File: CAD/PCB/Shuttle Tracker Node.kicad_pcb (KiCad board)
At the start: 2 copper layers, 90.8 x 45.7 mm, 23 parts, among them J1 Conn_01x01, J2 Conn_01x01, J3 Conn_01x01, J4 Conn_01x01, J5 Conn_01x01, J6 Conn_01x01, J7 Conn_01x01, SW1 SW_Push, SW10 SW_Push, SW11 SW_Push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

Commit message: Added Mounting Holes
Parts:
- added REF**: MountingHole_3.2mm_M3, MountingHole:MountingHole_3.2mm_M3, F.Cu at (128.5, 79.8)
- added REF**: MountingHole_3.2mm_M3, MountingHole:MountingHole_3.2mm_M3, F.Cu at (128.5, 118.4)
- added REF**: MountingHole_3.2mm_M3, MountingHole:MountingHole_3.2mm_M3, F.Cu at (226.6, 79.8)
- added REF**: MountingHole_3.2mm_M3, MountingHole:MountingHole_3.2mm_M3, F.Cu at (226.6, 118.4)
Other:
- board size 90.8 x 45.7 mm -> 105.2 x 45.7 mm
- board text added: "1.0.2"
- board text removed: "1.0.1"
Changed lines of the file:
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@@
     )
+  )
+  (footprint "MountingHole:MountingHole_3.2mm_M3" (layer "F.Cu")
+    (at 128.524 79.756)
+    (descr "Mounting Hole 3.2mm, no annular, M3")
+    (tags "mounting hole 3.2mm no annular m3")
+    (attr exclude_from_pos_files exclude_from_bom)
+    (fp_text reference "REF**" (at 0 -4.2) (layer "F.SilkS") hide
+      (effects (font (size 1 1) (thickness 0.15)))
+    )
+    (fp_text value "MountingHole_3.2mm_M3" (at 0 4.2) (layer "F.Fab")
+      (effects (font (size 1 1) (thickness 0.15)))
+    )
+    (fp_text user "${REFERENCE}" (at 0 0) (layer "F.Fab")
+      (effects (font (size 1 1) (thickness 0.15)))
+    )
+    (fp_circle (center 0 0) (end 3.2 0) (layer "Cmts.User") (width 0.15) (fill none))
+    (fp_circle (center 0 0) (end 3.45 0) (layer "F.CrtYd") (width 0.05) (fill none))
+    (pad "" np_thru_hole circle (at 0 0) (size 3.2 3.2) (drill 3.2) (layers F&B.Cu *.Mask))
+  )
+  (footprint "MountingHole:MountingHole_3.2mm_M3" (layer "F.Cu")
+    (at 128.524 118.364)
+    (descr "Mounting Hole 3.2mm, no annular, M3")
+    (tags "mounting hole 3.2mm no annular m3")
+    (attr exclude_from_pos_files exclude_from_bom)
+    (fp_text reference "REF**" (at 0 -4.2) (layer "F.SilkS") hide
+      (effects (font (size 1 1) (thickness 0.15)))
+    )
+    (fp_text value "MountingHole_3.2mm_M3" (at 0 4.2) (layer "F.Fab")
+      (effects (font (size 1 1) (thickness 0.15)))
+    )
+    (fp_text user "${REFERENCE}" (at 0 0) (layer "F.Fab")
+      (effects (font (size 1 1) (thickness 0.15)))
+    )
+    (fp_circle (center 0 0) (end 3.2 0) (layer "Cmts.User") (width 0.15) (fill none))
+    (fp_circle (center 0 0) (end 3.45 0) (layer "F.CrtYd") (width 0.05) (fill none))
+    (pad "" np_thru_hole circle (at 0 0) (size 3.2 3.2) (drill 3.2) (layers F&B.Cu *.Mask))
   )
   (footprint "B3F-1056:B3F-1056" (layer "F.Cu")
@@
     )
   )
+  (footprint "MountingHole:MountingHole_3.2mm_M3" (layer "F.Cu")
+    (at 226.568 79.756)
+    (descr "Mounting Hole 3.2mm, no annular, M3")
+    (tags "mounting hole 3.2mm no annular m3")
+    (attr exclude_from_pos_files exclude_from_bom)
+    (fp_text reference "REF**" (at 0 -4.2) (layer "F.SilkS") hide
+      (effects (font (size 1 1) (thickness 0.15)))
+    )
+    (fp_text value "MountingHole_3.2mm_M3" (at 0 4.2) (layer "F.Fab")
+      (effects (font (size 1 1) (thickness 0.15)))
+    )
+    (fp_text user "${REFERENCE}" (at 0 0) (layer "F.Fab")
+      (effects (font (size 1 1) (thickness 0.15)))
+    )
+    (fp_circle (center 0 0) (end 3.2 0) (layer "Cmts.User") (width 0.15) (fill none))
+    (fp_circle (center 0 0) (end 3.45 0) (layer "F.CrtYd") (width 0.05) (fill none))
+    (pad "" np_thru_hole circle (at 0 0) (size 3.2 3.2) (drill 3.2) (layers *.Cu *.Mask))
+  )
   (footprint "B3F-1056:B3F-1056" (layer "F.Cu")
     (at 171.45 96.8375)
@@
       (rotate (xyz 0 0 0))
     )
+  )
+  (footprint "MountingHole:MountingHole_3.2mm_M3" (layer "F.Cu")
+    (at 226.568 118.364)
+    (descr "Mounting Hole 3.2mm, no annular, M3")
+    (tags "mounting hole 3.2mm no annular m3")
+    (attr exclude_from_pos_files exclude_from_bom)
+    (fp_text reference "REF**" (at 0 -4.2) (layer "F.SilkS") hide
+      (effects (font (size 1 1) (thickness 0.15)))
+    )
+    (fp_text value "MountingHole_3.2mm_M3" (at 0 4.2) (layer "F.Fab")
+      (effects (font (size 1 1) (thickness 0.15)))
+    )
+    (fp_text user "${REFERENCE}" (at 0 0) (layer "F.Fab")
+      (effects (font (size 1 1) (thickness 0.15)))
+    )
+    (fp_circle (center 0 0) (end 3.2 0) (layer "Cmts.User") (width 0.15) (fill none))
+    (fp_circle (center 0 0) (end 3.45 0) (layer "F.CrtYd") (width 0.05) (fill none))
+    (pad "" np_thru_hole circle (at 0 0) (size 3.2 3.2) (drill 3.2) (layers F&B.Cu *.Mask))
   )
   (footprint "Resistor_THT:R_Axial_DIN0204_L3.6mm_D1.6mm_P5.08mm_Horizontal" (layer "B.Cu")
@@
       (xy 215.927615 106.759896)
     ) (layer "F.SilkS") (width 0) (fill solid))
-  (gr_line (start 222.885 119.38) (end 222.885 78.74) (layer "Edge.Cuts") (width 0.1))
-  (gr_arc (start 134.62 121.92) (mid 132.823949 121.176051) (end 132.08 119.38) (layer "Edge.Cuts") (width 0.1))
-  (gr_arc (start 220.345 76.2) (mid 222.141051 76.943949) (end 222.885 78.74) (layer "Edge.Cuts") (width 0.1))
-  (gr_arc (start 132.08 78.74) (mid 132.823949 76.943949) (end 134.62 76.2) (layer "Edge.Cuts") (width 0.1))
-  (gr_line (start 132.08 78.74) (end 132.08 119.38) (layer "Edge.Cuts") (width 0.1))
-  (gr_arc (start 222.885 119.38) (mid 222.141051 121.176051) (end 220.345 121.92) (layer "Edge.Cuts") (width 0.1))
-  (gr_line (start 220.345 76.2) (end 134.62 76.2) (layer "Edge.Cuts") (width 0.1))
-  (gr_line (start 134.62 121.92) (end 220.345 121.92) (layer "Edge.Cuts") (width 0.1))
-  (gr_text "1.0.1" (at 208.28 118.11) (layer "F.SilkS")
+  (gr_arc (start 226.568 114.808) (mid 230.124 118.364) (end 226.568 121.92) (layer "Edge.Cuts") (width 0.1))
+  (gr_arc (start 226.568 76.2) (mid 230.124 79.756) (end 226.568 83.312) (layer "Edge.Cuts") (width 0.1))
+  (gr_arc (start 128.524 83.312) (mid 124.968 79.756) (end 128.524 76.2) (layer "Edge.Cuts") (width 0.1))
+  (gr_line (start 226.568 114.808) (end 226.568 83.312) (layer "Edge.Cuts") (width 0.1))
+  (gr_line (start 128.524 83.312) (end 128.524 114.808) (layer "Edge.Cuts") (width 0.1))
+  (gr_arc (start 128.524 121.92) (mid 124.968 118.364) (end 128.524 114.808) (layer "Edge.Cuts") (width 0.1))
+  (gr_line (start 226.568 76.2) (end 128.524 76.2) (layer "Edge.Cuts") (width 0.1))
+  (gr_line (start 128.524 121.92) (end 226.568 121.92) (layer "Edge.Cuts") (width 0.1))
+  (gr_text "1.0.2" (at 208.28 118.11) (layer "F.SilkS")
     (effects (font (size 1 1) (thickness 0.15)))
   )

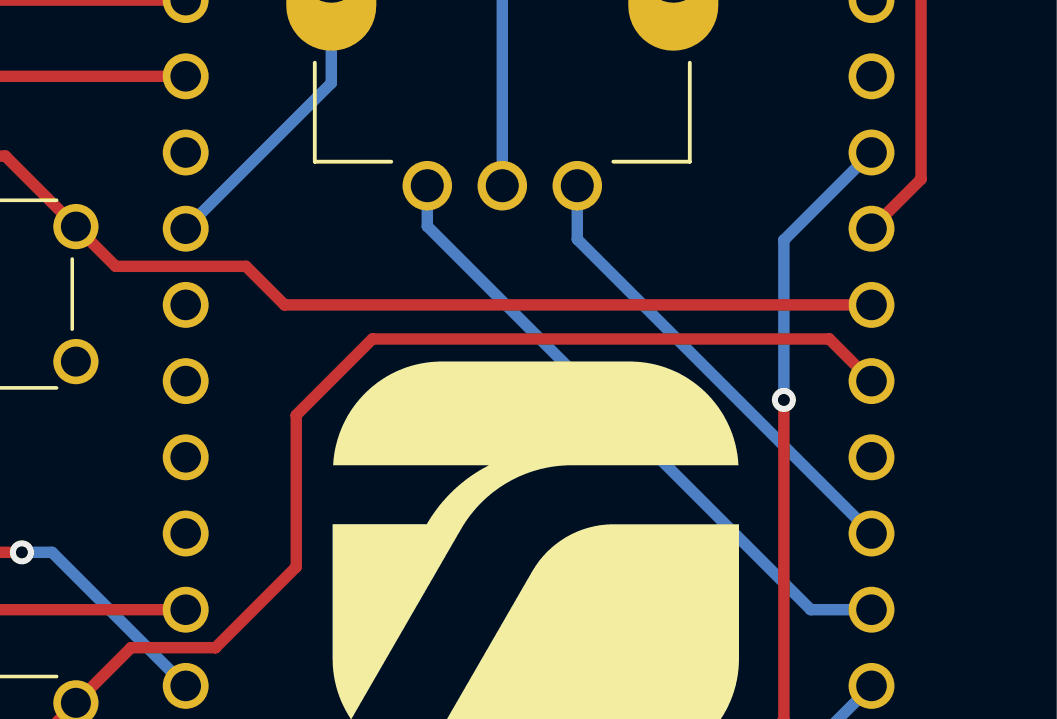
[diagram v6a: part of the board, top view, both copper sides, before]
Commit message: Changed IO Configuration
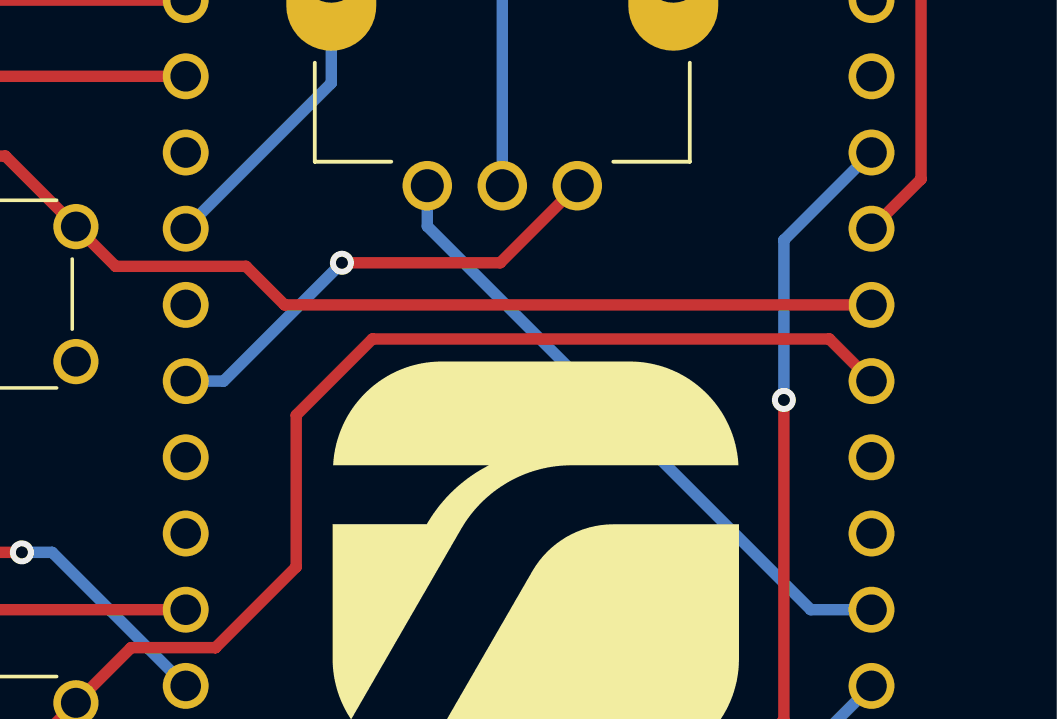
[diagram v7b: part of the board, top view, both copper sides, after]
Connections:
- U1 pad 11: ENC_B -> unconnected-(U1-Pad11)
- U1 pad 22: unconnected-(U1-Pad22) -> ENC_B
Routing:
- net ENC_B: track 15.7 -> 15.8 mm, vias 0 -> 1
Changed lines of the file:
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@@
   (net 24 "unconnected-(U1-Pad20)")
   (net 25 "unconnected-(U1-Pad21)")
-  (net 26 "unconnected-(U1-Pad22)")
-  (net 27 "unconnected-(U1-Pad23)")
-  (net 28 "unconnected-(U1-Pad25)")
-  (net 29 "ENC_GND_A")
-  (net 30 "BAT_5V")
-  (net 31 "BAT_GND")
+  (net 26 "unconnected-(U1-Pad23)")
+  (net 27 "unconnected-(U1-Pad25)")
+  (net 28 "ENC_GND_A")
+  (net 29 "BAT_5V")
+  (net 30 "BAT_GND")
+  (net 31 "unconnected-(U1-Pad11)")
   (footprint "Connector_Pin:Pin_D1.0mm_L10.0mm" (layer "F.Cu")
     (at 135.89 93.95 -90)
@@
     (fp_circle (center 0 0) (end 1 0) (layer "F.Fab") (width 0.12) (fill none))
     (pad "1" thru_hole circle (at 0 0 270) (size 2 2) (drill 1) (layers *.Cu *.Mask)
-      (net 30 "BAT_5V") (pinfunction "Pin_1") (pintype "passive"))
+      (net 29 "BAT_5V") (pinfunction "Pin_1") (pintype "passive"))
     (model "${KICAD6_3DMODEL_DIR}/Connector_Pin.3dshapes/Pin_D1.0mm_L10.0mm.wrl"
       (offset (xyz 0 0 0))
@@
     (fp_circle (center 0 0) (end 0.5 0) (layer "F.Fab") (width 0.12) (fill none))
     (pad "1" thru_hole circle (at 0 0 270) (size 2 2) (drill 1) (layers *.Cu *.Mask)
-      (net 31 "BAT_GND") (pinfunction "Pin_1") (pintype "passive"))
+      (net 30 "BAT_GND") (pinfunction "Pin_1") (pintype "passive"))
     (model "${KICAD6_3DMODEL_DIR}/Connector_Pin.3dshapes/Pin_D1.0mm_L10.0mm.wrl"
       (offset (xyz 0 0 0))
@@
       (net 13 "ENC_B") (pinfunction "B") (pintype "passive"))
     (pad "C" thru_hole circle (at 0 7.5) (size 1.65 1.65) (drill 1.1) (layers *.Cu *.Mask)
-      (net 29 "ENC_GND_A") (pinfunction "C") (pintype "passive"))
+      (net 28 "ENC_GND_A") (pinfunction "C") (pintype "passive"))
     (pad "S1" thru_hole oval (at -5.7 0) (size 3 6) (drill oval 2 2.8) (layers *.Cu *.Mask)
       (net 14 "ENC_SW_IN") (pinfunction "S1") (pintype "passive"))
@@
       (net 20 "unconnected-(U1-Pad10)") (pinfunction "GND") (pintype "power_in"))
     (pad "11" thru_hole circle (at -11.43 -8.0078 180) (size 1.53 1.53) (drill 1.02) (layers *.Cu *.Mask)
-      (net 13 "ENC_B") (pinfunction "GPIO8") (pintype "bidirectional"))
+      (net 31 "unconnected-(U1-Pad11)") (pinfunction "GPIO8") (pintype "bidirectional"))
     (pad "12" thru_hole circle (at -11.43 -10.5478 180) (size 1.53 1.53) (drill 1.02) (layers *.Cu *.Mask)
       (net 12 "ENC_A") (pinfunction "GPIO9") (pintype "bidirectional"))
@@
       (net 3 "LCD_5V") (pinfunction "5V") (pintype "power_in"))
     (pad "14" thru_hole circle (at -11.43 -15.6278 180) (size 1.53 1.53) (drill 1.02) (layers *.Cu *.Mask)
-      (net 30 "BAT_5V") (pinfunction "5V") (pintype "power_in"))
+      (net 29 "BAT_5V") (pinfunction "5V") (pintype "power_in"))
     (pad "15" thru_hole circle (at -11.43 -18.1678 180) (size 1.53 1.53) (drill 1.02) (layers *.Cu *.Mask)
-      (net 31 "BAT_GND") (pinfunction "GND") (pintype "power_in"))
+      (net 30 "BAT_GND") (pinfunction "GND") (pintype "power_in"))
     (pad "16" thru_hole circle (at 11.43 -18.1678 180) (size 1.53 1.53) (drill 1.02) (layers *.Cu *.Mask)
       (net 4 "LCD_GND") (pinfunction "GND") (pintype "power_in"))
@@
       (net 25 "unconnected-(U1-Pad21)") (pinfunction "GPIO21/U0TXD") (pintype "bidirectional"))
     (pad "22" thru_hole circle (at 11.43 -2.9278 180) (size 1.53 1.53) (drill 1.02) (layers *.Cu *.Mask)
-      (net 26 "unconnected-(U1-Pad22)") (pinfunction "GPIO20/U0RXD") (pintype "bidirectional"))
+      (net 13 "ENC_B") (pinfunction "GPIO20/U0RXD") (pintype "bidirectional"))
     (pad "23" thru_hole circle (at 11.43 -0.3878 180) (size 1.53 1.53) (drill 1.02) (layers *.Cu *.Mask)
-      (net 27 "unconnected-(U1-Pad23)") (pinfunction "GND") (pintype "power_in"))
+      (net 26 "unconnected-(U1-Pad23)") (pinfunction "GND") (pintype "power_in"))
     (pad "24" thru_hole circle (at 11.43 2.1522 180) (size 1.53 1.53) (drill 1.02) (layers *.Cu *.Mask)
       (net 14 "ENC_SW_IN") (pinfunction "GPIO10") (pintype "bidirectional"))
     (pad "25" thru_hole circle (at 11.43 4.6922 180) (size 1.53 1.53) (drill 1.02) (layers *.Cu *.Mask)
-      (net 28 "unconnected-(U1-Pad25)") (pinfunction "GND") (pintype "power_in"))
+      (net 27 "unconnected-(U1-Pad25)") (pinfunction "GND") (pintype "power_in"))
     (pad "26" thru_hole circle (at 11.43 7.2322 180) (size 1.53 1.53) (drill 1.02) (layers *.Cu *.Mask)
       (net 5 "C1") (pinfunction "GPIO3") (pintype "bidirectional"))
@@
       (net 9 "C4") (pinfunction "GPIO0/XTAL_32K_P") (pintype "bidirectional"))
     (pad "30" thru_hole circle (at 11.43 17.3922 180) (size 1.53 1.53) (drill 1.02) (layers *.Cu *.Mask)
-      (net 29 "ENC_GND_A") (pinfunction "GND") (pintype "power_in"))
+      (net 28 "ENC_GND_A") (pinfunction "GND") (pintype "power_in"))
   )
   (gr_poly
@@
   (segment (start 205.537501 95.475001) (end 205.537501 96.825501) (width 0.381) (layer "B.Cu") (net 12))
   (segment (start 205.537501 96.825501) (end 218.3198 109.6078) (width 0.381) (layer "B.Cu") (net 12))
-  (segment (start 210.537501 95.475001) (end 210.537501 97.260301) (width 0.381) (layer "B.Cu") (net 13))
-  (segment (start 210.537501 97.260301) (end 220.345 107.0678) (width 0.381) (layer "B.Cu") (net 13))
+  (segment (start 210.537501 95.475001) (end 207.968502 98.044) (width 0.381) (layer "F.Cu") (net 13))
+  (segment (start 207.968502 98.044) (end 202.692 98.044) (width 0.381) (layer "F.Cu") (net 13))
+  (via (at 202.692 98.044) (size 0.8) (drill 0.4) (layers "F.Cu" "B.Cu") (net 13))
+  (segment (start 202.692 98.044) (end 198.7482 101.9878) (width 0.381) (layer "B.Cu") (net 13))
+  (segment (start 198.7482 101.9878) (end 197.485 101.9878) (width 0.381) (layer "B.Cu") (net 13))
   (segment (start 202.337501 87.975001) (end 202.337501 92.055299) (width 0.381) (layer "B.Cu") (net 14))
   (segment (start 202.337501 92.055299) (end 197.485 96.9078) (width 0.381) (layer "B.Cu") (net 14))
@@
   (segment (start 152.4 112.395) (end 154.6928 114.6878) (width 0.381) (layer "B.Cu") (net 23))
   (segment (start 154.6928 114.6878) (end 197.485 114.6878) (width 0.381) (layer "B.Cu") (net 23))
-  (segment (start 203.0798 81.6678) (end 197.485 81.6678) (width 0.381) (layer "F.Cu") (net 29))
-  (segment (start 203.2 81.788) (end 203.0798 81.6678) (width 0.381) (layer "F.Cu") (net 29))
-  (via (at 203.2 81.788) (size 0.8) (drill 0.4) (layers "F.Cu" "B.Cu") (net 29))
-  (segment (start 208.037501 95.475001) (end 208.037501 86.625501) (width 0.381) (layer "B.Cu") (net 29))
-  (segment (start 208.037501 86.625501) (end 203.2 81.788) (width 0.381) (layer "B.Cu") (net 29))
-  (segment (start 219.964 120.904) (end 221.996 118.872) (width 0.381) (layer "F.Cu") (net 30))
-  (segment (start 132.725652 104.386894) (end 132.684681 104.427865) (width 0.381) (layer "F.Cu") (net 30))
-  (segment (start 135.62 99.32) (end 132.725652 102.214348) (width 0.381) (layer "F.Cu") (net 30))
-  (segment (start 132.725652 102.214348) (end 132.725652 104.386894) (width 0.381) (layer "F.Cu") (net 30))
-  (segment (start 132.684681 104.427865) (end 132.684681 114.904681) (width 0.381) (layer "F.Cu") (net 30))
-  (segment (start 138.684 120.904) (end 219.964 120.904) (width 0.381) (layer "F.Cu") (net 30))
-  (segment (start 221.996 118.872) (end 221.996 116.3388) (width 0.381) (layer "F.Cu") (net 30))
-  (segment (start 221.996 116.3388) (end 220.345 114.6878) (width 0.381) (layer "F.Cu") (net 30))
-  (segment (start 132.684681 114.904681) (end 138.684 120.904) (width 0.381) (layer "F.Cu") (net 30))
-  (segment (start 133.446681 105.543319) (end 133.446681 113.634681) (width 0.381) (layer "F.Cu") (net 31))
-  (segment (start 133.446681 113.634681) (end 139.7 119.888) (width 0.381) (layer "F.Cu") (net 31))
-  (segment (start 135.62 103.37) (end 133.446681 105.543319) (width 0.381) (layer "F.Cu") (net 31))
-  (segment (start 217.6848 119.888) (end 220.345 117.2278) (width 0.381) (layer "F.Cu") (net 31))
-  (segment (start 139.7 119.888) (end 217.6848 119.888) (width 0.381) (layer "F.Cu") (net 31))
+  (segment (start 203.0798 81.6678) (end 197.485 81.6678) (width 0.381) (layer "F.Cu") (net 28))
+  (segment (start 203.2 81.788) (end 203.0798 81.6678) (width 0.381) (layer "F.Cu") (net 28))
+  (via (at 203.2 81.788) (size 0.8) (drill 0.4) (layers "F.Cu" "B.Cu") (net 28))
+  (segment (start 208.037501 95.475001) (end 208.037501 86.625501) (width 0.381) (layer "B.Cu") (net 28))
+  (segment (start 208.037501 86.625501) (end 203.2 81.788) (width 0.381) (layer "B.Cu") (net 28))
+  (segment (start 219.964 120.904) (end 221.996 118.872) (width 0.381) (layer "F.Cu") (net 29))
+  (segment (start 132.725652 104.386894) (end 132.684681 104.427865) (width 0.381) (layer "F.Cu") (net 29))
+  (segment (start 135.62 99.32) (end 132.725652 102.214348) (width 0.381) (layer "F.Cu") (net 29))
+  (segment (start 132.725652 102.214348) (end 132.725652 104.386894) (width 0.381) (layer "F.Cu") (net 29))
+  (segment (start 132.684681 104.427865) (end 132.684681 114.904681) (width 0.381) (layer "F.Cu") (net 29))
+  (segment (start 138.684 120.904) (end 219.964 120.904) (width 0.381) (layer "F.Cu") (net 29))
+  (segment (start 221.996 118.872) (end 221.996 116.3388) (width 0.381) (layer "F.Cu") (net 29))
+  (segment (start 221.996 116.3388) (end 220.345 114.6878) (width 0.381) (layer "F.Cu") (net 29))
+  (segment (start 132.684681 114.904681) (end 138.684 120.904) (width 0.381) (layer "F.Cu") (net 29))
+  (segment (start 133.446681 105.543319) (end 133.446681 113.634681) (width 0.381) (layer "F.Cu") (net 30))
+  (segment (start 133.446681 113.634681) (end 139.7 119.888) (width 0.381) (layer "F.Cu") (net 30))
+  (segment (start 135.62 103.37) (end 133.446681 105.543319) (width 0.381) (layer "F.Cu") (net 30))
+  (segment (start 217.6848 119.888) (end 220.345 117.2278) (width 0.381) (layer "F.Cu") (net 30))
+  (segment (start 139.7 119.888) (end 217.6848 119.888) (width 0.381) (layer "F.Cu") (net 30))
   (group "" (id 639b4e34-dd1b-4ec8-9119-ffca7ddfe66d)
     (members
